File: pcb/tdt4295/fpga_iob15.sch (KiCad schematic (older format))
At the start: 8 parts, among them U102 XC7A100T-FTG256-tdt4295

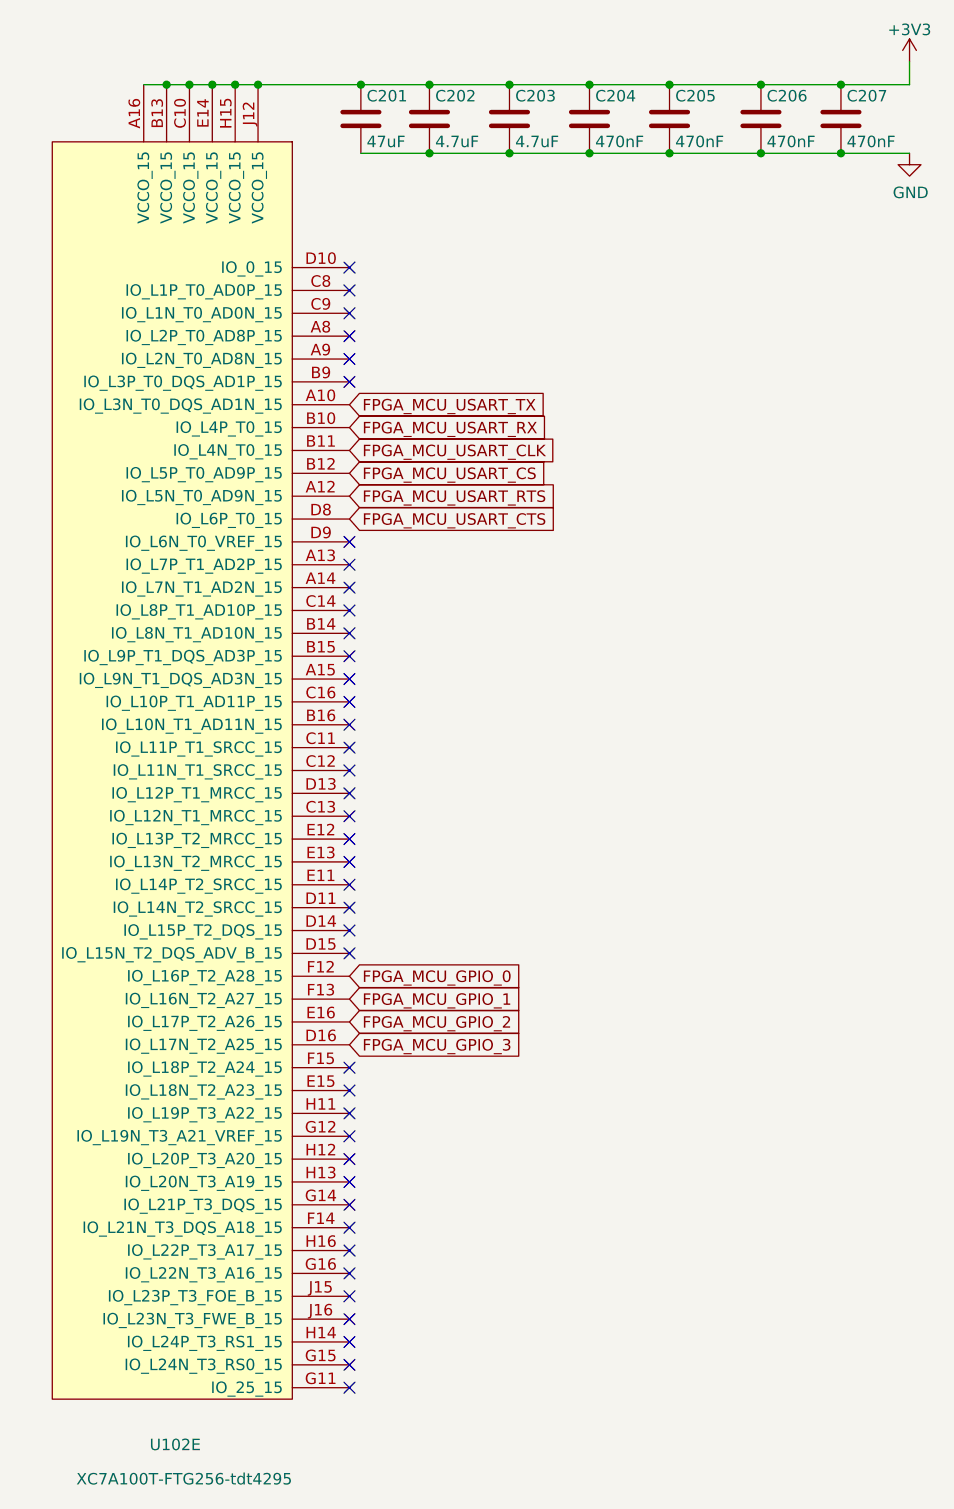
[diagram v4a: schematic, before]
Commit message: associate (some) footprints to the symbols
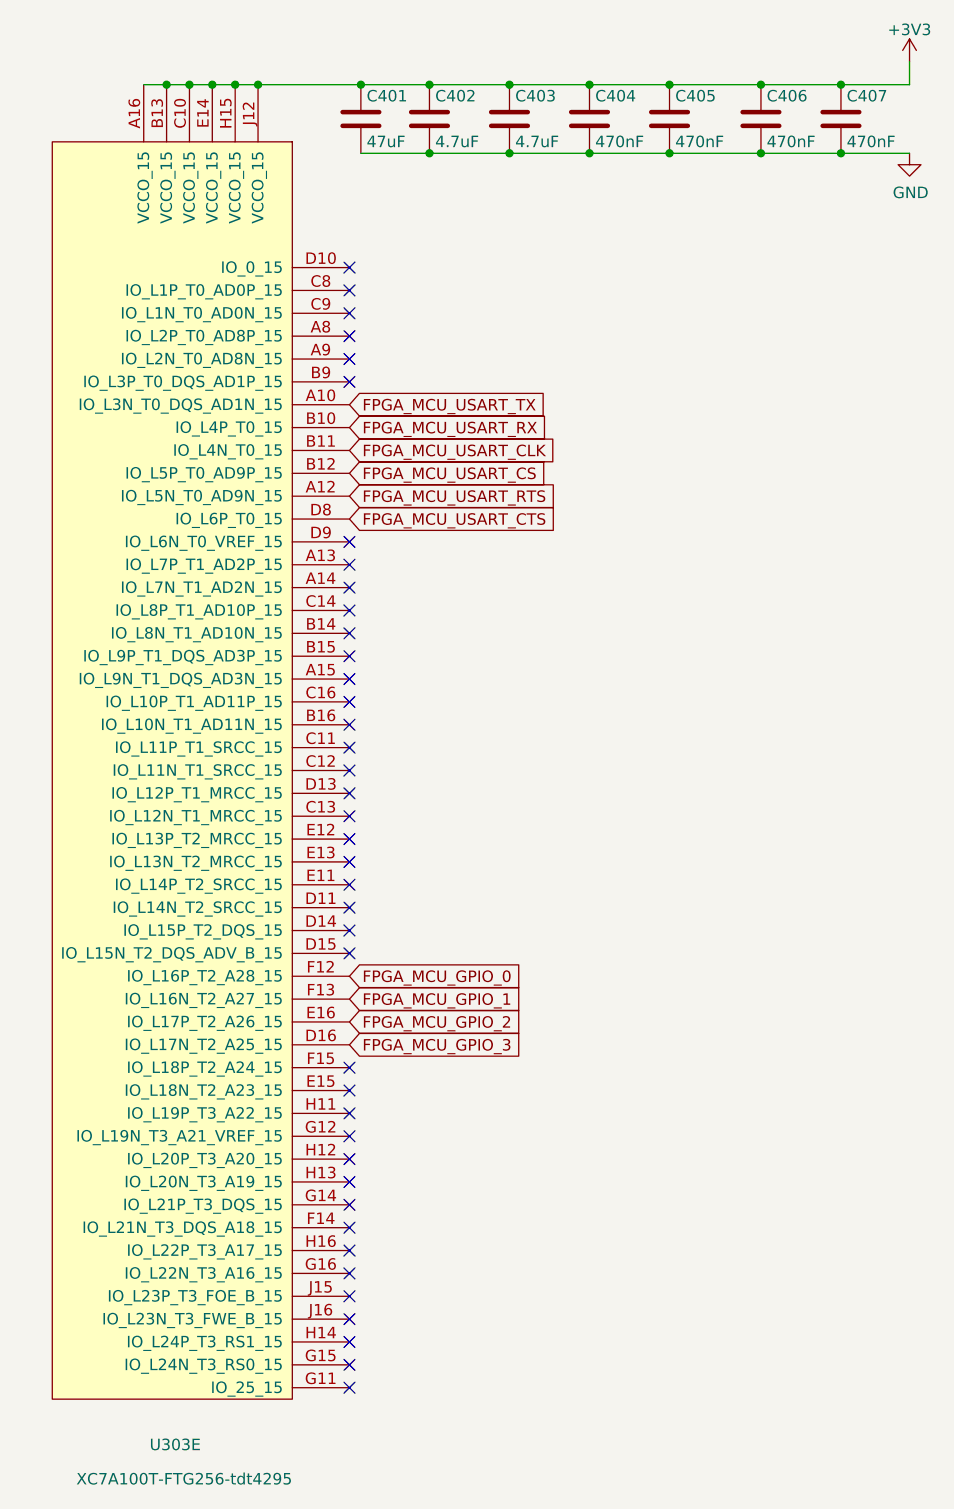
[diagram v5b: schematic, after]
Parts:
- C401: renamed from C201; DK_Detail_Page (none) -> https://www.digikey.no/product-detail/no/murata-electronics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
- C402: renamed from C202; Component name (none) -> C2012X7R1A475K125AC; DK_Detail_Page (none) -> https://www.digikey.no/product-detail/no/tdk-corporation/C2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
- C403: renamed from C203; Component name (none) -> C2012X7R1A475K125AC; DK_Detail_Page (none) -> https://www.digikey.no/product-detail/no/tdk-corporation/C2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
- renumbered C204 to C404, C205 to C405, C206 to C406, C207 to C407, U102 to U303
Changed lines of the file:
@@
 $EndDescr
 $Comp
-L xc7a100t-ftg256-modified:XC7A100T-FTG256-tdt4295 U102
+L xc7a100t-ftg256-modified:XC7A100T-FTG256-tdt4295 U303
 U 5 1 614C09B5
 P 1700 4050
-F 0 "U102" H 1700 1250 50  0000 R CNN
+F 0 "U303" H 1700 1250 50  0000 R CNN
 F 1 "XC7A100T-FTG256-tdt4295" H 2100 1100 50  0000 R CNN
 F 2 "Package_BGA:Xilinx_FTG256" H 1700 1000 50  0001 C CNN
@@
 Connection ~ 1950 900
 $Comp
-L power:GND #PWR0202
+L power:GND #PWR0402
 U 1 1 614E24A1
 P 4800 1200
-F 0 "#PWR0202" H 4800 950 50  0001 C CNN
+F 0 "#PWR0402" H 4800 950 50  0001 C CNN
 F 1 "GND" H 4805 1027 50  0000 C CNN
 F 2 "" H 4800 1200 50  0001 C CNN
@@
 P 2400 1050
 AR Path="/61459CB7/615F1C9B" Ref="C?"  Part="1"
-AR Path="/614933B1/615F1C9B" Ref="C201"  Part="1"
-AR Path="/617F72AC/614933B1/615F1C9B" Ref="C201"  Part="1"
-F 0 "C201" H 2425 1150 50  0000 L CNN
+AR Path="/614933B1/615F1C9B" Ref="C?"  Part="1"
+AR Path="/617F72AC/614933B1/615F1C9B" Ref="C401"  Part="1"
+F 0 "C401" H 2425 1150 50  0000 L CNN
 F 1 "47uF" H 2425 950 50  0000 L CNN
 F 2 "Capacitor_SMD:C_1210_3225Metric_Pad1.33x2.70mm_HandSolder" H 2438 900 50  0001 C CNN
 F 3 "https://www.farnell.com/datasheets/2047839.pdf" H 2400 1050 50  0001 C CNN
 F 4 "GRM32ER71A476ME15L" H 2400 1050 50  0001 C CNN "Component name"
+F 5 "https://www.digikey.no/product-detail/no/murata-electronics/GRM32ER71A476ME15L/490-6543-1-ND/3845740" H 2400 1050 50  0001 C CNN "DK_Detail_Page"
 	1    2400 1050
 	1    0    0    -1
@@
 P 2700 1050
 AR Path="/61459CB7/615F1CA1" Ref="C?"  Part="1"
-AR Path="/614933B1/615F1CA1" Ref="C202"  Part="1"
-AR Path="/617F72AC/614933B1/615F1CA1" Ref="C202"  Part="1"
-F 0 "C202" H 2725 1150 50  0000 L CNN
+AR Path="/614933B1/615F1CA1" Ref="C?"  Part="1"
+AR Path="/617F72AC/614933B1/615F1CA1" Ref="C402"  Part="1"
+F 0 "C402" H 2725 1150 50  0000 L CNN
 F 1 "4.7uF" H 2725 950 50  0000 L CNN
 F 2 "Capacitor_SMD:C_0805_2012Metric_Pad1.18x1.45mm_HandSolder" H 2738 900 50  0001 C CNN
-F 3 "~" H 2700 1050 50  0001 C CNN
+F 3 "" H 2700 1050 50  0001 C CNN
+F 4 "C2012X7R1A475K125AC" H 2700 1050 50  0001 C CNN "Component name"
+F 5 "" H 2700 1050 50  0001 C CNN "DK_Datasheet_Link"
+F 6 "https://www.digikey.no/product-detail/no/tdk-corporation/C2012X7R1A475K125AC/445-7591-1-ND/2733663" H 2700 1050 50  0001 C CNN "DK_Detail_Page"
 	1    2700 1050
 	1    0    0    -1
@@
 P 3050 1050
 AR Path="/61459CB7/615F1CA7" Ref="C?"  Part="1"
-AR Path="/614933B1/615F1CA7" Ref="C203"  Part="1"
-AR Path="/617F72AC/614933B1/615F1CA7" Ref="C203"  Part="1"
-F 0 "C203" H 3075 1150 50  0000 L CNN
+AR Path="/614933B1/615F1CA7" Ref="C?"  Part="1"
+AR Path="/617F72AC/614933B1/615F1CA7" Ref="C403"  Part="1"
+F 0 "C403" H 3075 1150 50  0000 L CNN
 F 1 "4.7uF" H 3075 950 50  0000 L CNN
 F 2 "Capacitor_SMD:C_0805_2012Metric_Pad1.18x1.45mm_HandSolder" H 3088 900 50  0001 C CNN
-F 3 "~" H 3050 1050 50  0001 C CNN
+F 3 "" H 3050 1050 50  0001 C CNN
+F 4 "C2012X7R1A475K125AC" H 3050 1050 50  0001 C CNN "Component name"
+F 5 "" H 3050 1050 50  0001 C CNN "DK_Datasheet_Link"
+F 6 "https://www.digikey.no/product-detail/no/tdk-corporation/C2012X7R1A475K125AC/445-7591-1-ND/2733663" H 3050 1050 50  0001 C CNN "DK_Detail_Page"
 	1    3050 1050
 	1    0    0    -1
@@
 P 3400 1050
 AR Path="/61459CB7/615F1CAD" Ref="C?"  Part="1"
-AR Path="/614933B1/615F1CAD" Ref="C204"  Part="1"
-AR Path="/617F72AC/614933B1/615F1CAD" Ref="C204"  Part="1"
-F 0 "C204" H 3425 1150 50  0000 L CNN
+AR Path="/614933B1/615F1CAD" Ref="C?"  Part="1"
+AR Path="/617F72AC/614933B1/615F1CAD" Ref="C404"  Part="1"
+F 0 "C404" H 3425 1150 50  0000 L CNN
 F 1 "470nF" H 3425 950 50  0000 L CNN
 F 2 "Capacitor_SMD:C_0603_1608Metric_Pad1.08x0.95mm_HandSolder" H 3438 900 50  0001 C CNN
@@
 P 3750 1050
 AR Path="/61459CB7/615F1CB3" Ref="C?"  Part="1"
-AR Path="/614933B1/615F1CB3" Ref="C205"  Part="1"
-AR Path="/617F72AC/614933B1/615F1CB3" Ref="C205"  Part="1"
-F 0 "C205" H 3775 1150 50  0000 L CNN
+AR Path="/614933B1/615F1CB3" Ref="C?"  Part="1"
+AR Path="/617F72AC/614933B1/615F1CB3" Ref="C405"  Part="1"
+F 0 "C405" H 3775 1150 50  0000 L CNN
 F 1 "470nF" H 3775 950 50  0000 L CNN
 F 2 "Capacitor_SMD:C_0603_1608Metric_Pad1.08x0.95mm_HandSolder" H 3788 900 50  0001 C CNN
@@
 P 4150 1050
 AR Path="/61459CB7/615F1CB9" Ref="C?"  Part="1"
-AR Path="/614933B1/615F1CB9" Ref="C206"  Part="1"
-AR Path="/617F72AC/614933B1/615F1CB9" Ref="C206"  Part="1"
-F 0 "C206" H 4175 1150 50  0000 L CNN
+AR Path="/614933B1/615F1CB9" Ref="C?"  Part="1"
+AR Path="/617F72AC/614933B1/615F1CB9" Ref="C406"  Part="1"
+F 0 "C406" H 4175 1150 50  0000 L CNN
 F 1 "470nF" H 4175 950 50  0000 L CNN
 F 2 "Capacitor_SMD:C_0603_1608Metric_Pad1.08x0.95mm_HandSolder" H 4188 900 50  0001 C CNN
@@
 P 4500 1050
 AR Path="/61459CB7/615F1CBF" Ref="C?"  Part="1"
-AR Path="/614933B1/615F1CBF" Ref="C207"  Part="1"
-AR Path="/617F72AC/614933B1/615F1CBF" Ref="C207"  Part="1"
-F 0 "C207" H 4525 1150 50  0000 L CNN
+AR Path="/614933B1/615F1CBF" Ref="C?"  Part="1"
+AR Path="/617F72AC/614933B1/615F1CBF" Ref="C407"  Part="1"
+F 0 "C407" H 4525 1150 50  0000 L CNN
 F 1 "470nF" H 4525 950 50  0000 L CNN
 F 2 "Capacitor_SMD:C_0603_1608Metric_Pad1.08x0.95mm_HandSolder" H 4538 900 50  0001 C CNN
@@
 	4800 900  4800 800
 $Comp
-L power:+3V3 #PWR0201
+L power:+3V3 #PWR0401
 U 1 1 61732788
 P 4800 800
-F 0 "#PWR0201" H 4800 650 50  0001 C CNN
+F 0 "#PWR0401" H 4800 650 50  0001 C CNN
 F 1 "+3V3" H 4800 940 50  0000 C CNN
 F 2 "" H 4800 800 50  0001 C CNN

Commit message: correct capacitor values, make junctions for IOB34&35
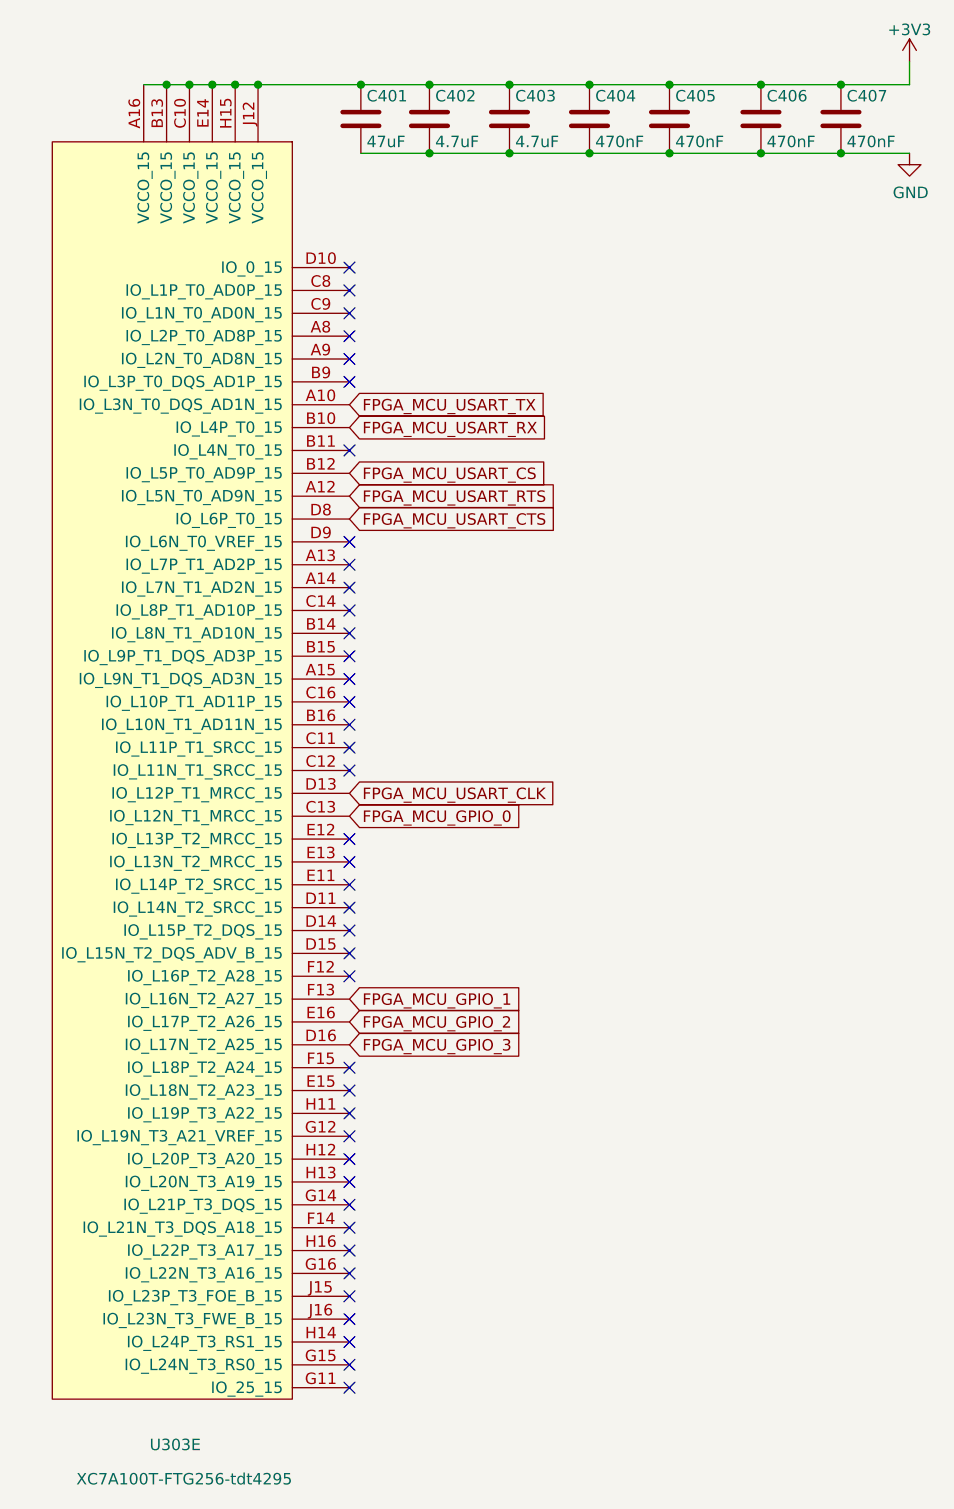
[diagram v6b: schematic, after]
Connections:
- net FPGA_MCU_GPIO_0: now also U303.C13 (IO_L12N_T1_MRCC_15); no longer U303.F12 (IO_L16P_T2_A28_15)
- net FPGA_MCU_USART_CLK: now also U303.D13 (IO_L12P_T1_MRCC_15); no longer U303.B11 (IO_L4N_T0_15)
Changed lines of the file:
@@
 $EndDescr
-$Comp
-L xc7a100t-ftg256-modified:XC7A100T-FTG256-tdt4295 U303
-U 5 1 614C09B5
-P 1700 4050
-F 0 "U303" H 1700 1250 50  0000 R CNN
-F 1 "XC7A100T-FTG256-tdt4295" H 2100 1100 50  0000 R CNN
-F 2 "Package_BGA:Xilinx_FTG256" H 1700 1000 50  0001 C CNN
-F 3 "" H 1700 1000 50  0000 C CNN
-	5    1700 4050
-	1    0    0    -1
-$EndComp
-Wire Wire Line
-	1450 900  1550 900
-Connection ~ 1550 900
-Wire Wire Line
-	1550 900  1650 900
-Connection ~ 1650 900
-Wire Wire Line
-	1650 900  1750 900
-Connection ~ 1750 900
-Wire Wire Line
-	1750 900  1850 900
-Connection ~ 1850 900
-Wire Wire Line
-	1850 900  1950 900
-Connection ~ 1950 900
 $Comp
 L power:GND #PWR0402
@@
 Text GLabel 2350 2300 2    50   Input ~ 0
 FPGA_MCU_USART_TX
-Text GLabel 2350 2500 2    50   Input ~ 0
+Text GLabel 2350 4000 2    50   Input ~ 0
 FPGA_MCU_USART_CLK
 Text GLabel 2350 2400 2    50   Input ~ 0
@@
 Text GLabel 2350 2800 2    50   Input ~ 0
 FPGA_MCU_USART_CTS
-Text GLabel 2350 4800 2    50   Input ~ 0
+Text GLabel 2350 4100 2    50   Input ~ 0
 FPGA_MCU_GPIO_0
 Text GLabel 2350 4900 2    50   Input ~ 0
@@
 Wire Wire Line
 	2400 1200 2700 1200
-Wire Wire Line
-	1950 900  2400 900
 Connection ~ 2400 900
 Wire Wire Line
@@
 NoConn ~ 2350 3800
 NoConn ~ 2350 3900
-NoConn ~ 2350 4000
-NoConn ~ 2350 4100
+NoConn ~ 2350 2500
 NoConn ~ 2350 4200
 NoConn ~ 2350 4300
@@
 NoConn ~ 2350 5400
 NoConn ~ 2350 5500
+Wire Wire Line
+	1950 900  2400 900
+Connection ~ 1950 900
+Wire Wire Line
+	1850 900  1950 900
+Connection ~ 1850 900
+Wire Wire Line
+	1750 900  1850 900
+Connection ~ 1750 900
+Wire Wire Line
+	1650 900  1750 900
+Connection ~ 1650 900
+Wire Wire Line
+	1450 900  1550 900
+Wire Wire Line
+	1550 900  1650 900
+Connection ~ 1550 900
+$Comp
+L xc7a100t-ftg256-modified:XC7A100T-FTG256-tdt4295 U303
+U 5 1 614C09B5
+P 1700 4050
+F 0 "U303" H 1700 1250 50  0000 R CNN
+F 1 "XC7A100T-FTG256-tdt4295" H 2100 1100 50  0000 R CNN
+F 2 "Package_BGA:Xilinx_FTG256" H 1700 1000 50  0001 C CNN
+F 3 "" H 1700 1000 50  0000 C CNN
+	5    1700 4050
+	1    0    0    -1
+$EndComp
+NoConn ~ 2350 4800
 $EndSCHEMATC

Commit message: add footprints, rename components
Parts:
- C404, C405, C406, C407: DK_Detail_Page (none) -> https://www.digikey.no/product-detail/en/murata-electronics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
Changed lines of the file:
@@
 F 3 "https://www.farnell.com/datasheets/2048812.pdf" H 3400 1050 50  0001 C CNN
 F 4 "GRM188R71C474KA88D" H 3400 1050 50  0001 C CNN "Component name"
+F 5 "https://www.digikey.no/product-detail/en/murata-electronics/GRM188R71C474KA88D/490-3295-1-ND/702836" H 3400 1050 50  0001 C CNN "DK_Detail_Page"
 	1    3400 1050
 	1    0    0    -1
@@
 F 3 "https://www.farnell.com/datasheets/2048812.pdf" H 3750 1050 50  0001 C CNN
 F 4 "GRM188R71C474KA88D" H 3750 1050 50  0001 C CNN "Component name"
+F 5 "https://www.digikey.no/product-detail/en/murata-electronics/GRM188R71C474KA88D/490-3295-1-ND/702836" H 3750 1050 50  0001 C CNN "DK_Detail_Page"
 	1    3750 1050
 	1    0    0    -1
@@
 F 3 "https://www.farnell.com/datasheets/2048812.pdf" H 4150 1050 50  0001 C CNN
 F 4 "GRM188R71C474KA88D" H 4150 1050 50  0001 C CNN "Component name"
+F 5 "https://www.digikey.no/product-detail/en/murata-electronics/GRM188R71C474KA88D/490-3295-1-ND/702836" H 4150 1050 50  0001 C CNN "DK_Detail_Page"
 	1    4150 1050
 	1    0    0    -1
@@
 F 3 "https://www.farnell.com/datasheets/2048812.pdf" H 4500 1050 50  0001 C CNN
 F 4 "GRM188R71C474KA88D" H 4500 1050 50  0001 C CNN "Component name"
+F 5 "https://www.digikey.no/product-detail/en/murata-electronics/GRM188R71C474KA88D/490-3295-1-ND/702836" H 4500 1050 50  0001 C CNN "DK_Detail_Page"
 	1    4500 1050
 	1    0    0    -1

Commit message: add digikey part numbers, create BOM
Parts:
- C401: Digi-Key_PN (none) -> 490-6543-1-ND
- C402, C403: Digi-Key_PN (none) -> 445-7591-1-ND
- C404, C405, C406, C407: Digi-Key_PN (none) -> 490-3295-1-ND
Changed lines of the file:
@@
 F 4 "GRM32ER71A476ME15L" H 2400 1050 50  0001 C CNN "Component name"
 F 5 "https://www.digikey.no/product-detail/no/murata-electronics/GRM32ER71A476ME15L/490-6543-1-ND/3845740" H 2400 1050 50  0001 C CNN "DK_Detail_Page"
+F 6 "490-6543-1-ND" H 2400 1050 50  0001 C CNN "Digi-Key_PN"
 	1    2400 1050
 	1    0    0    -1
@@
 F 5 "" H 2700 1050 50  0001 C CNN "DK_Datasheet_Link"
 F 6 "https://www.digikey.no/product-detail/no/tdk-corporation/C2012X7R1A475K125AC/445-7591-1-ND/2733663" H 2700 1050 50  0001 C CNN "DK_Detail_Page"
+F 7 "445-7591-1-ND" H 2700 1050 50  0001 C CNN "Digi-Key_PN"
 	1    2700 1050
 	1    0    0    -1
@@
 F 5 "" H 3050 1050 50  0001 C CNN "DK_Datasheet_Link"
 F 6 "https://www.digikey.no/product-detail/no/tdk-corporation/C2012X7R1A475K125AC/445-7591-1-ND/2733663" H 3050 1050 50  0001 C CNN "DK_Detail_Page"
+F 7 "445-7591-1-ND" H 3050 1050 50  0001 C CNN "Digi-Key_PN"
 	1    3050 1050
 	1    0    0    -1
@@
 F 4 "GRM188R71C474KA88D" H 3400 1050 50  0001 C CNN "Component name"
 F 5 "https://www.digikey.no/product-detail/en/murata-electronics/GRM188R71C474KA88D/490-3295-1-ND/702836" H 3400 1050 50  0001 C CNN "DK_Detail_Page"
+F 6 "490-3295-1-ND" H 3400 1050 50  0001 C CNN "Digi-Key_PN"
 	1    3400 1050
 	1    0    0    -1
@@
 F 4 "GRM188R71C474KA88D" H 3750 1050 50  0001 C CNN "Component name"
 F 5 "https://www.digikey.no/product-detail/en/murata-electronics/GRM188R71C474KA88D/490-3295-1-ND/702836" H 3750 1050 50  0001 C CNN "DK_Detail_Page"
+F 6 "490-3295-1-ND" H 3750 1050 50  0001 C CNN "Digi-Key_PN"
 	1    3750 1050
 	1    0    0    -1
@@
 F 4 "GRM188R71C474KA88D" H 4150 1050 50  0001 C CNN "Component name"
 F 5 "https://www.digikey.no/product-detail/en/murata-electronics/GRM188R71C474KA88D/490-3295-1-ND/702836" H 4150 1050 50  0001 C CNN "DK_Detail_Page"
+F 6 "490-3295-1-ND" H 4150 1050 50  0001 C CNN "Digi-Key_PN"
 	1    4150 1050
 	1    0    0    -1
@@
 F 4 "GRM188R71C474KA88D" H 4500 1050 50  0001 C CNN "Component name"
 F 5 "https://www.digikey.no/product-detail/en/murata-electronics/GRM188R71C474KA88D/490-3295-1-ND/702836" H 4500 1050 50  0001 C CNN "DK_Detail_Page"
+F 6 "490-3295-1-ND" H 4500 1050 50  0001 C CNN "Digi-Key_PN"
 	1    4500 1050
 	1    0    0    -1
